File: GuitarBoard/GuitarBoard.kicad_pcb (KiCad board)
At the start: 2 copper layers, 100 x 45 mm, 50 parts, among them IC1 CD4069UBE, Q1 2N3904, Q2 2N3904, SW1 Amp Knob Switch

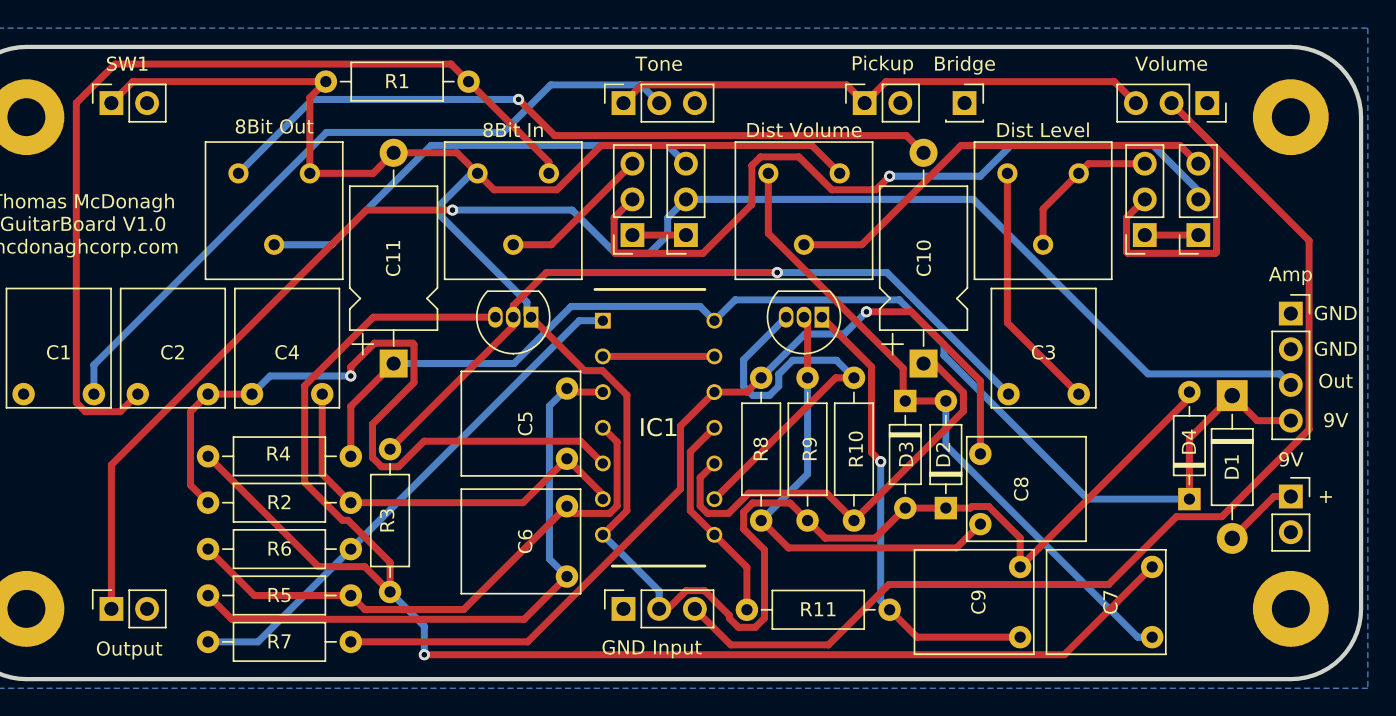
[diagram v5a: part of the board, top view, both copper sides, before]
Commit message: Switched which pedal came first. Added JLC order number location
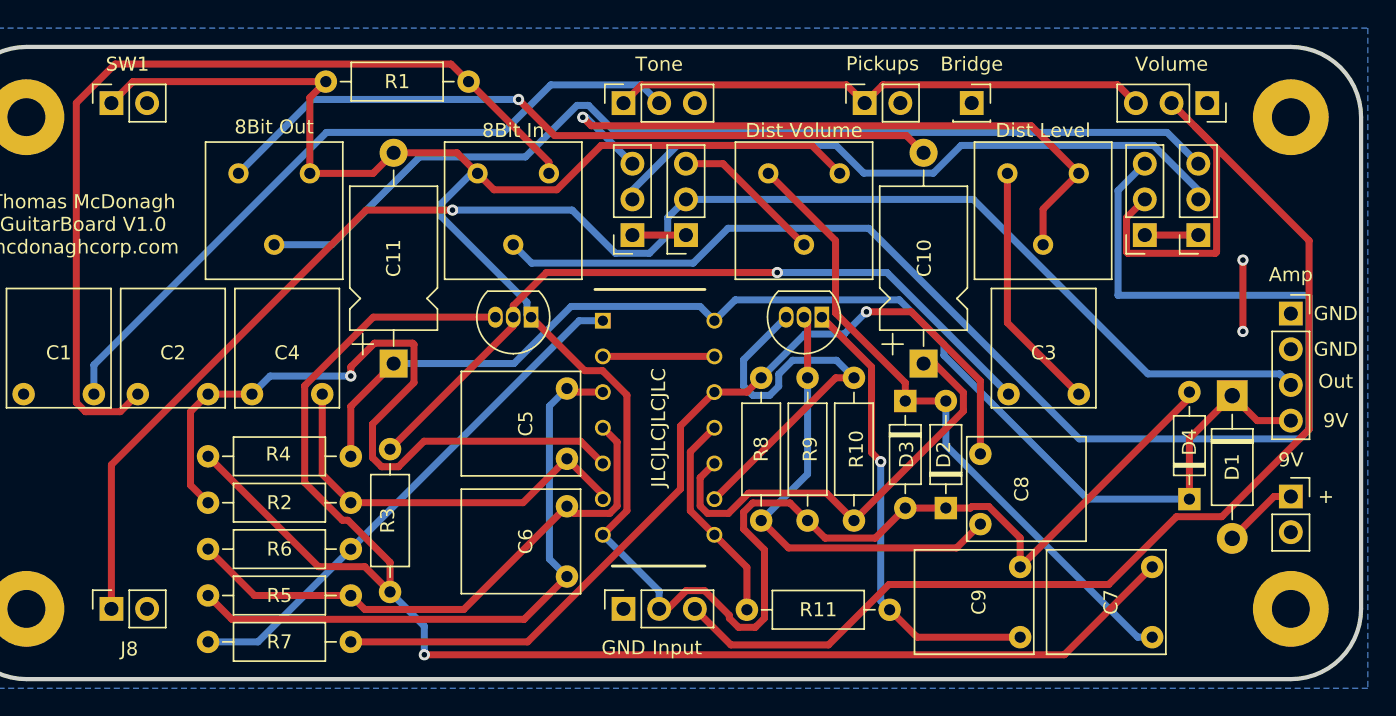
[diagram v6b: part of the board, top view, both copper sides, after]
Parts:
- moved Bridge 0.51 mm to (129.3, 79.0)
- renumbered Output to J8, IC1 to JLCJLCJLCJLC, Pickup to Pickups, A to SW2, B to SW3, A to SW4, B to SW5
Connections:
- 8Bit In pad 2: FXInB -> FXInA
- 8Bit Out pad 2: FXOutB -> FXOutA
- Dist Level pad 2: FXInA -> FXInB
- Dist Level pad 3: FXInA -> FXInB
- Dist Volume pad 2: FXOutA -> FXOutB
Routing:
- net FXInA: track 11.1 -> 98.0 mm
- net FXOutA: track 31.5 -> 71.6 mm
- net FXInB: track 10.9 -> 48.0 mm, vias 0 -> 1
- net FXOutB: track 32.8 -> 10.8 mm
- net Net-(SW3-Pad2): track 54.6 -> 46.5 mm, vias 1 -> 0
- net GND: track 0.00 -> 5.08 mm, vias 0 -> 2
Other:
- board text added: "REV A"

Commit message: Minor change
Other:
- board text removed: "REV A"

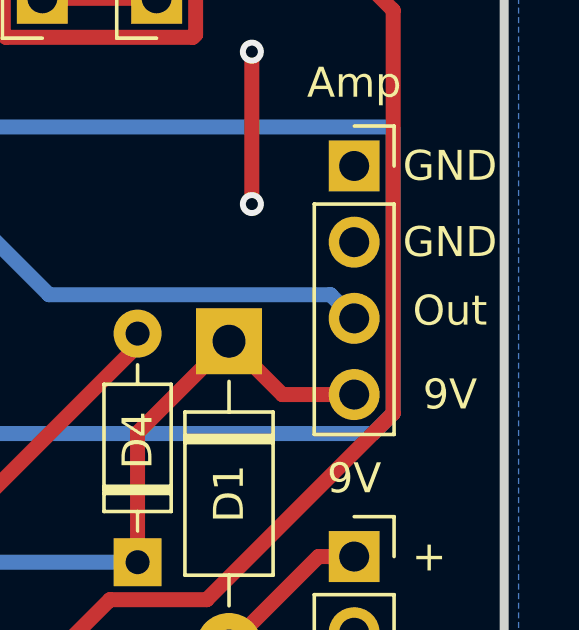
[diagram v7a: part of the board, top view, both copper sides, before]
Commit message: Starting new board and fixed minor silkscreen error in GuitarBoard
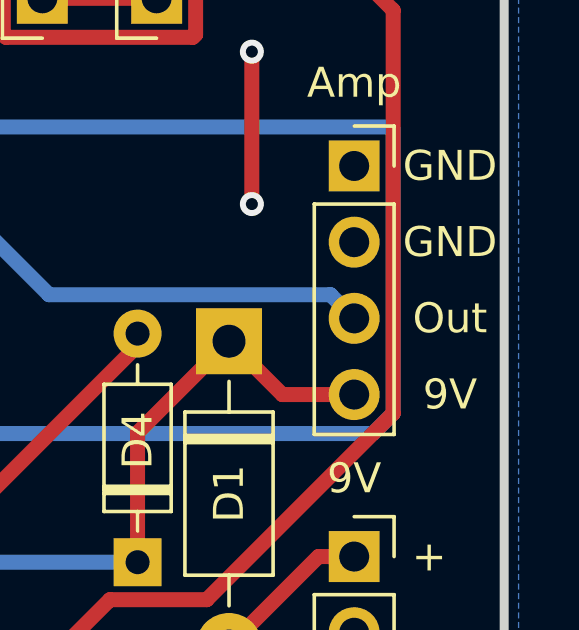
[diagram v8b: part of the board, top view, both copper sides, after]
